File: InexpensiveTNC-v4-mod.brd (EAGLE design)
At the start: 100 x 92.7 mm, 46 parts, among them IC1 78L05Z, J4 GPS, T1 BC846BSMD, U1 PIC16F88, X1 20MHz, X2 332-02, X3 332-02

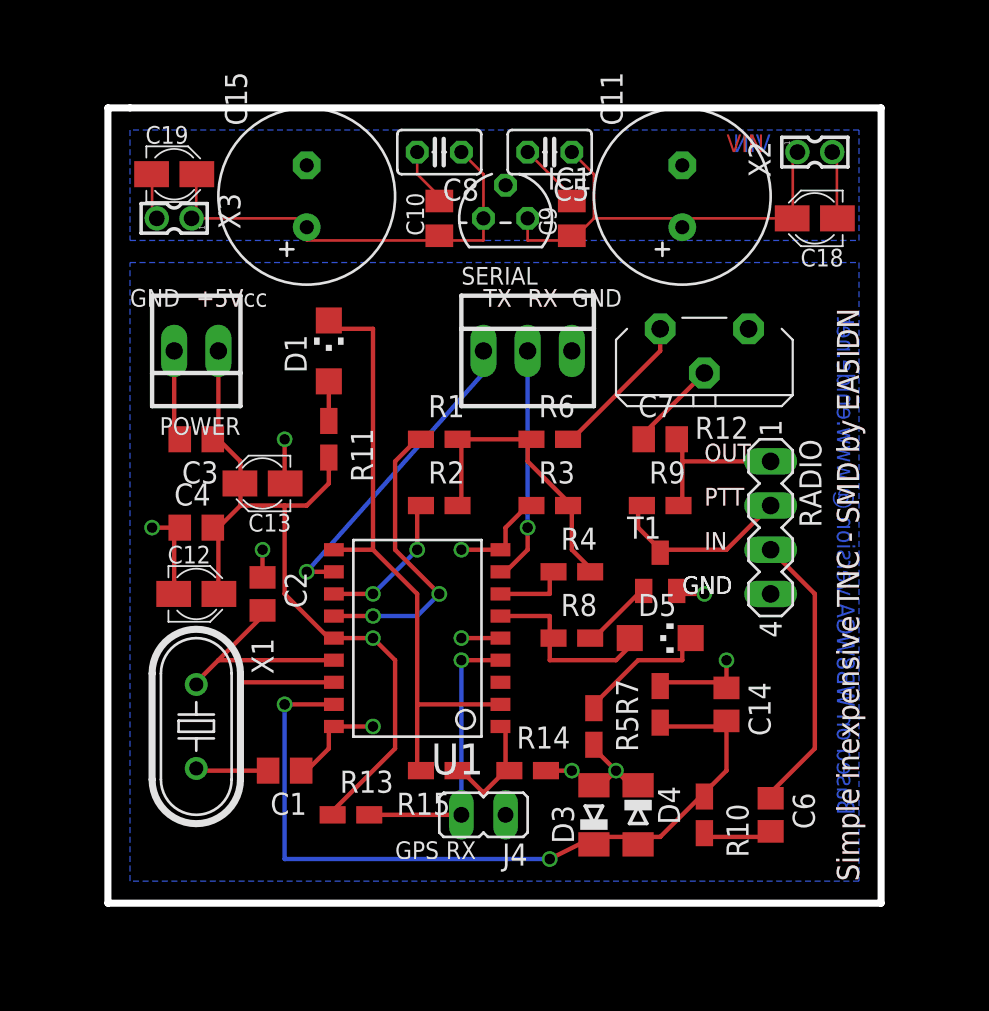
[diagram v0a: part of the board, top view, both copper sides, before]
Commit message: Traces widened, generated some gerblers for ITEAD studio
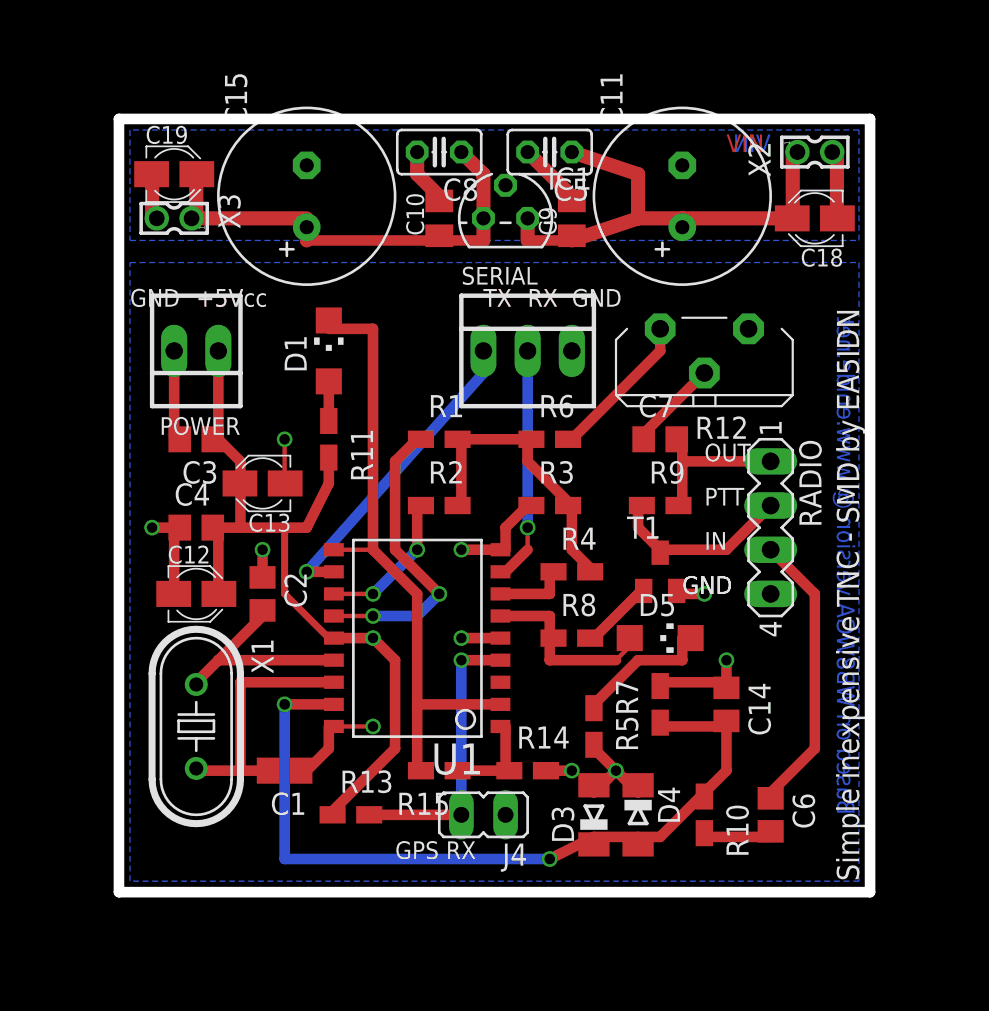
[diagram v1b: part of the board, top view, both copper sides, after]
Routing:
- net VREG-VIN: track 26.2 -> 28.1 mm
- net N$29: track 6.86 -> 5.81 mm
- net VCC: track 46.5 -> 47.0 mm
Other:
- outline, holes or cut-outs redrawn
